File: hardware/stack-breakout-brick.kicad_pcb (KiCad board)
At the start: 2 copper layers, 40 x 40 mm, 10 parts, among them J1 STACK-UP-1, J2 STACK-DOWN-1, J3 STACK-UP-2, J4 STACK-DOWN-2, J5 CON-SERVO, J6 CON-SERVO, U1 DRILL, U2 DRILL, U3 DRILL, U4 DRILL

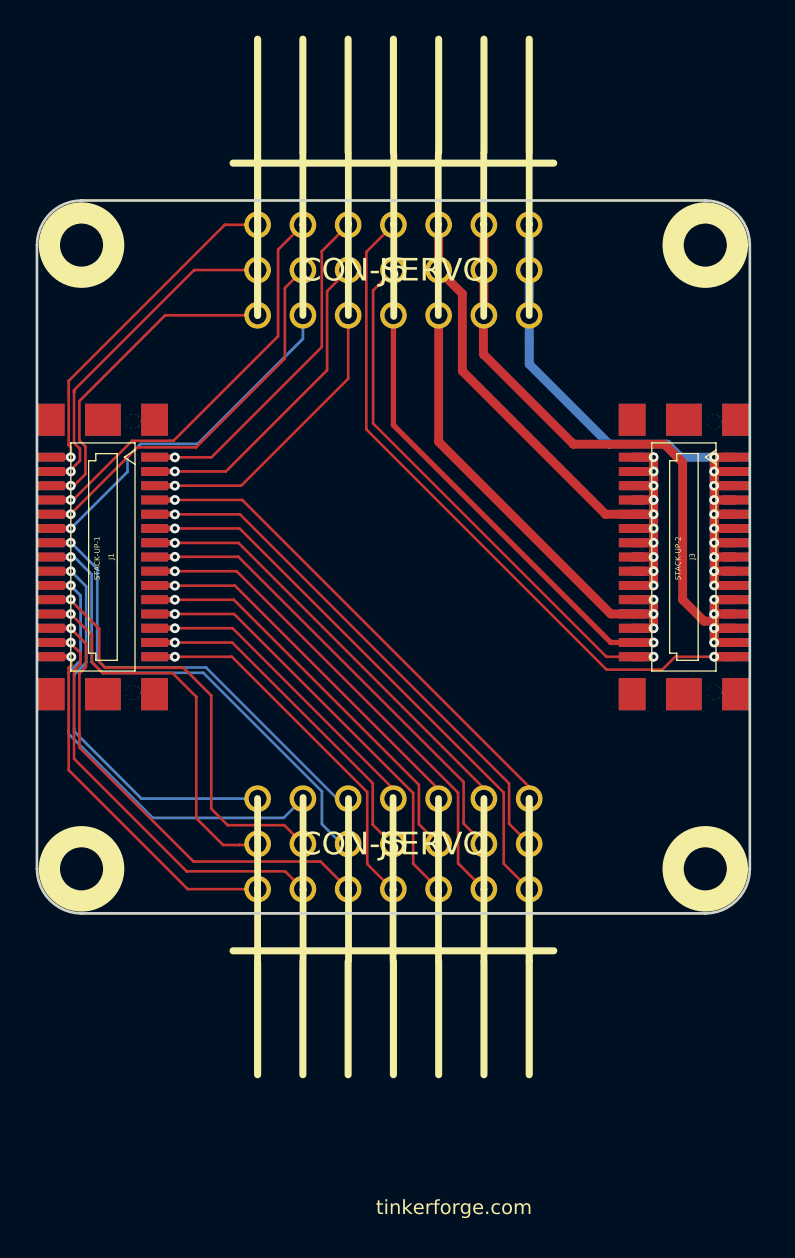
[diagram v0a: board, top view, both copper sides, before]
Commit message: Add pin labeling
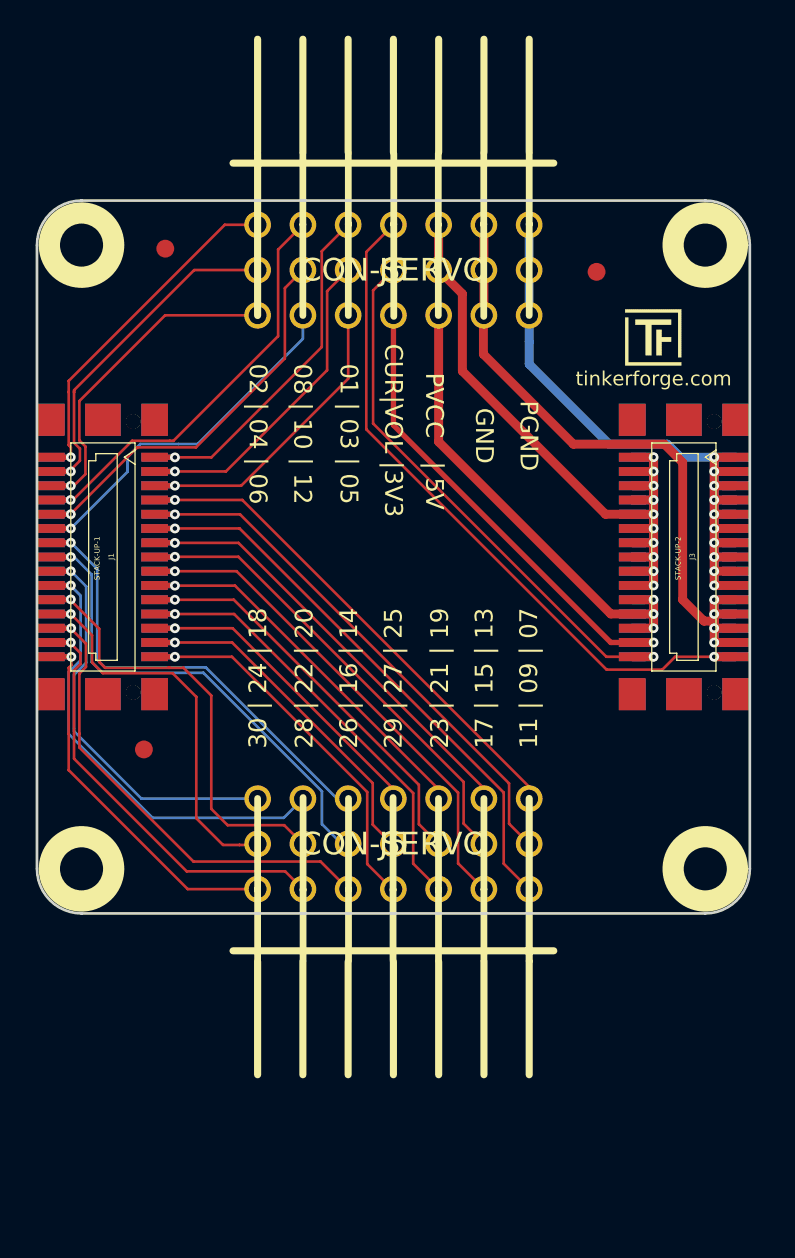
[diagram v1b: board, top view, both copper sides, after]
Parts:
- added Fiducial_Mark: VAL**, kicad-libraries:Fiducial_Mark, F.Cu at (125.5, 111.6)
- added Fiducial_Mark: VAL**, kicad-libraries:Fiducial_Mark, F.Cu at (150.9, 84.8)
- added Fiducial_Mark: VAL**, kicad-libraries:Fiducial_Mark, F.Cu at (126.7, 83.5)
- added G***: Logo_31x31, kicad-libraries:Logo_31x31, F.Cu at (152.5, 86.9)
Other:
- board text added: "01 | 03 | 05"
- board text added: "02 | 04 | 06"
- board text added: "08 | 10 | 12"
- board text added: "11 | 09 | 07"
- board text added: "17 | 15 | 13"
- board text added: "23 | 21 | 19"
- board text added: "26 | 16 | 14"
- board text added: "28 | 22 | 20"
- board text added: "29 | 27 | 25"
- board text added: "30 | 24 | 18"
- board text added: "CUR|VOL |3V3"
- board text added: "GND"
- board text added: "PGND"
- board text added: "PVCC | 5V"

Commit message: Add product name labeling
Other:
- board text added: "Stack Breakout Brick 1.0"
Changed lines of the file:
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@@
     (area 119.424999 80.724999 159.575001 120.875001)
     (thickness 1.6)
-    (drawings 23)
+    (drawings 24)
     (tracks 511)
     (zones 0)
@@
       (clearance 0.65024))
   )
+  (gr_text "Stack Breakout\nBrick 1.0" (at 153.9 112.9) (layer F.SilkS)
+    (effects (font (size 0.8 0.8) (thickness 0.15)))
+  )
   (gr_text PGND (at 147.1 94 270) (layer F.SilkS)

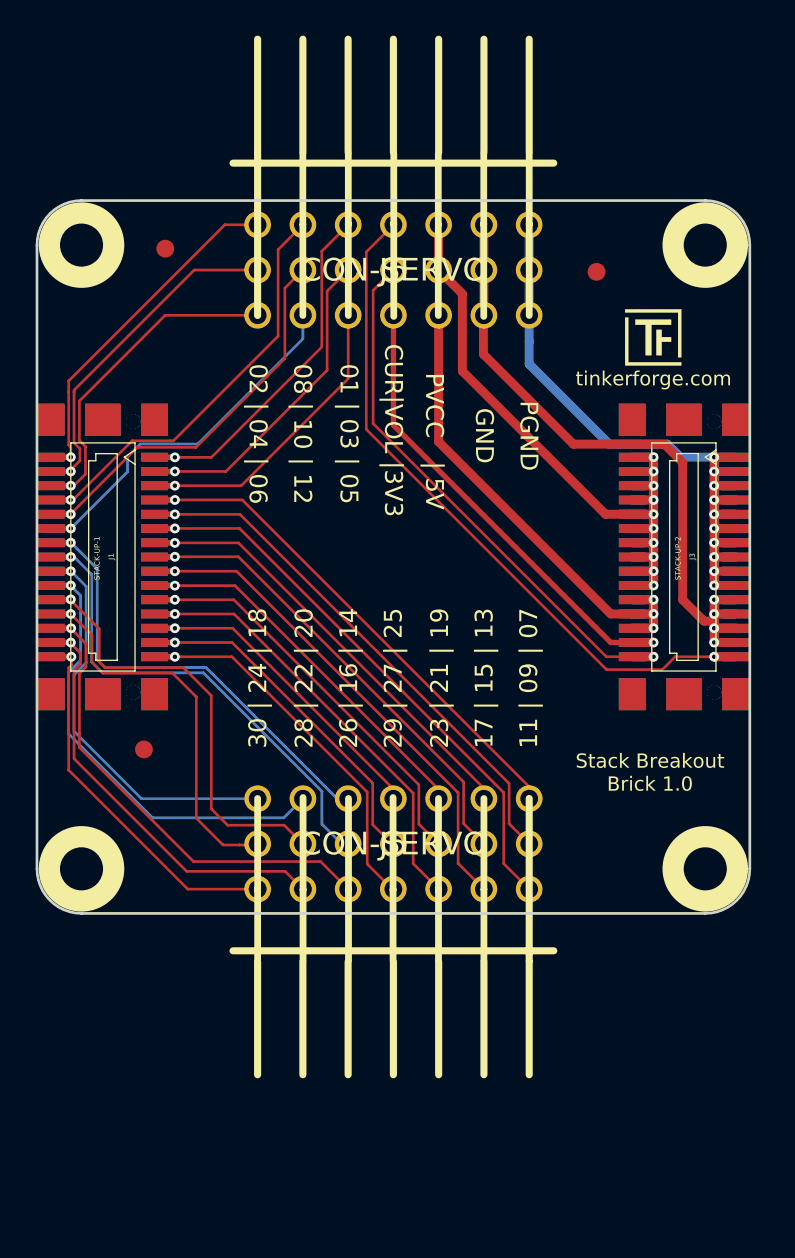
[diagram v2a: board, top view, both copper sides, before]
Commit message: Fix labeling and routing
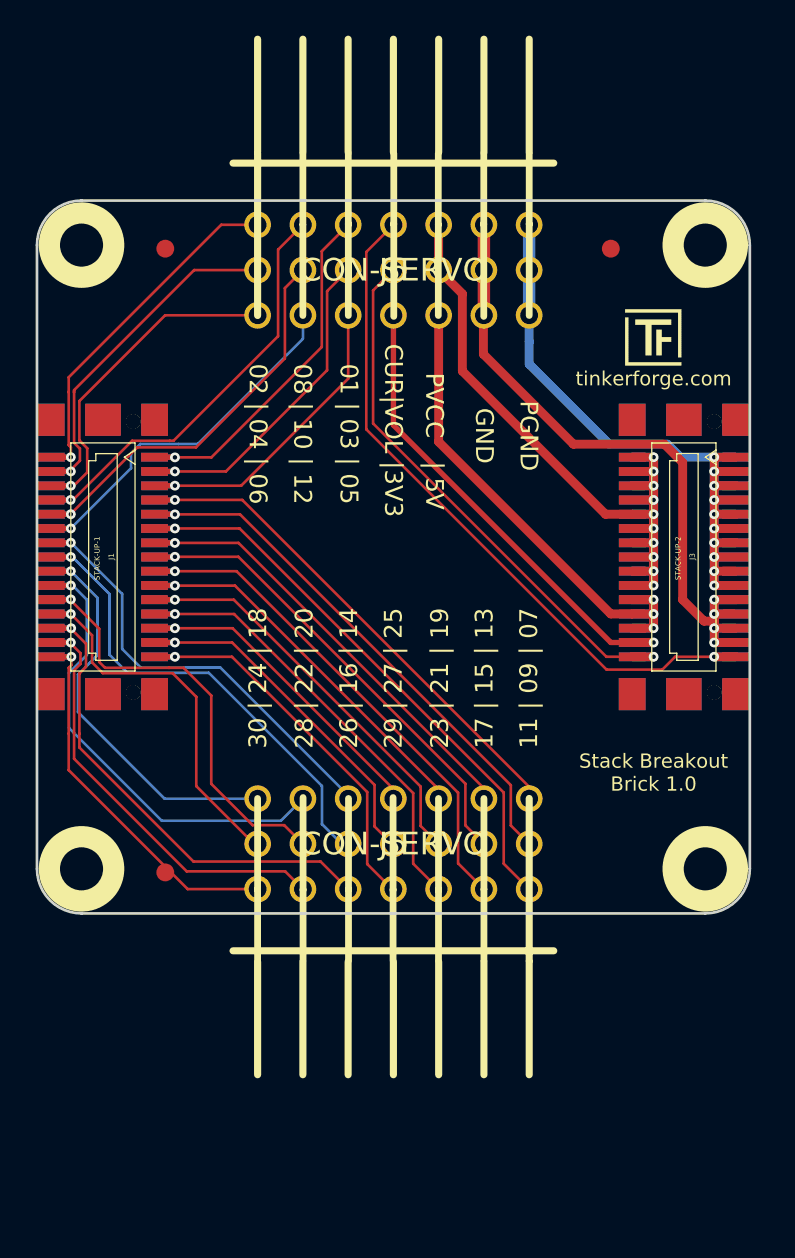
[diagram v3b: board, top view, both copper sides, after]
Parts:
- moved Fiducial_Mark 7.00 mm to (126.7, 118.5)
- moved Fiducial_Mark 1.53 mm to (151.7, 83.5)
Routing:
- net EX-SEL-01: track 23.0 -> 21.8 mm
- net EX-SEL-00: track 26.5 -> 25.7 mm
- net SEL-04: track 26.7 -> 25.9 mm
- net SEL-05: track 28.9 -> 28.2 mm

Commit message: Fix fiducial marks
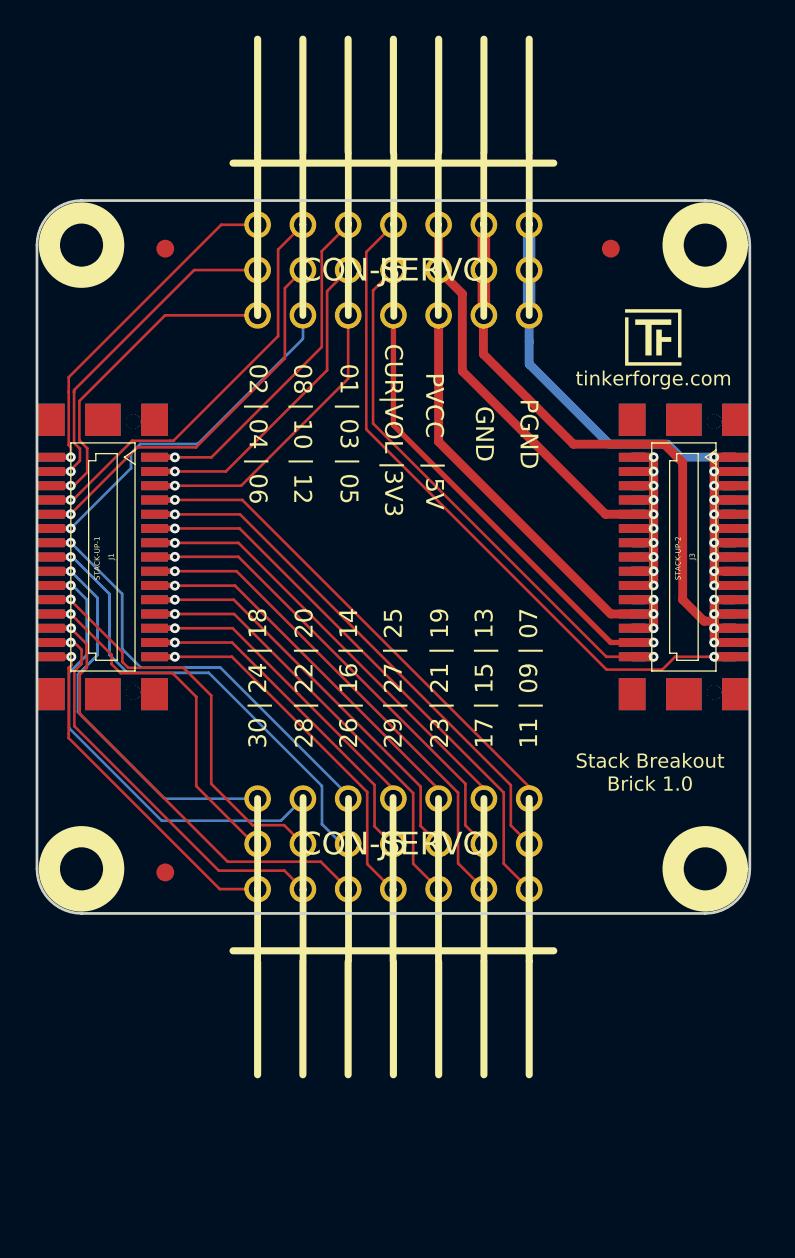
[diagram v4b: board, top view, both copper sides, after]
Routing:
- net EX-SER2-RXD: track 27.8 -> 26.7 mm
- net EX-SER2-RTS: track 22.2 -> 21.2 mm
- net EX-SER2-TXD: track 25.0 -> 24.0 mm
- net EX-SEL-00: track 25.7 -> 24.9 mm
- net EX-SEL-01: track 21.8 -> 21.2 mm
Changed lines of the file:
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@@
     (thickness 1.6)
     (drawings 24)
-    (tracks 505)
+    (tracks 503)
     (zones 0)
     (modules 14)
@@
   (title_block
     (title "Stack Breakout Brick")
-    (date 2017-03-01)
+    (date 2017-03-02)
     (rev 1.0)
     (company "Tinkerforge GmbH")
     (comment 1 "Licensed under CERN OHL v.1.1")
-    (comment 2 "Copyright (©) 2017, L.lauer <lukas.lauer@fh-bielefeld.de>")
+    (comment 2 "Copyright (©) 2017, L.Lauer <lukas.lauer@fh-bielefeld.de>")
   )
   (layers
@@
   )
   (setup
-    (last_trace_width 0.7)
+    (last_trace_width 0.25)
     (user_trace_width 0.15)
     (user_trace_width 0.2)
@@
     (effects (font (size 0.8 0.8) (thickness 0.15)))
   )
-  (gr_text "Stack Breakout\nBrick 1.0" (at 154.1 112.9) (layer F.SilkS)
+  (gr_text "Stack Breakout\nBrick 1.0" (at 153.9 112.9) (layer F.SilkS)
     (effects (font (size 0.8 0.8) (thickness 0.15)))
   )
-  (gr_text PGND (at 147.1 94 270) (layer F.SilkS)
+  (gr_text PGND (at 147.1 93.9 270) (layer F.SilkS)
     (effects (font (size 1 1) (thickness 0.2)))
   )
-  (gr_text GND (at 144.6 94 270) (layer F.SilkS)
+  (gr_text GND (at 144.6 93.9 270) (layer F.SilkS)
     (effects (font (size 1 1) (thickness 0.2)))
   )
@@
   (segment (start 127.724266 107.02) (end 129.28 108.575734) (width 0.15) (layer F.Cu) (net 27))
   (segment (start 121.4 103.18) (end 121.4 103.24) (width 0.15) (layer F.Cu) (net 27))
-  (segment (start 123.320002 107.02) (end 126.9 107.02) (width 0.15) (layer F.Cu) (net 27))
+  (segment (start 124.620002 107.02) (end 126.9 107.02) (width 0.15) (layer F.Cu) (net 27))
   (segment (start 126.9 107.02) (end 126.93 107.02) (width 0.15) (layer F.Cu) (net 27))
-  (segment (start 122.992133 106.692131) (end 123.320002 107.02) (width 0.15) (layer F.Cu) (net 27))
-  (segment (start 122.992133 104.832133) (end 122.992133 106.692131) (width 0.15) (layer F.Cu) (net 27))
-  (segment (start 121.4 103.24) (end 122.992133 104.832133) (width 0.15) (layer F.Cu) (net 27))
+  (segment (start 124.292133 106.692131) (end 124.620002 107.02) (width 0.15) (layer F.Cu) (net 27))
+  (segment (start 124.292133 106.132133) (end 124.292133 106.692131) (width 0.15) (layer F.Cu) (net 27))
+  (segment (start 121.4 103.24) (end 124.292133 106.132133) (width 0.15) (layer F.Cu) (net 27))
   (segment (start 120.31962 103.18) (end 121.4 103.18) (width 0.3) (layer B.Cu) (net 27))
   (segment (start 121.38224 103.19776) (end 121.4 103.18) (width 0.3) (layer F.Cu) (net 27))
@@
   (segment (start 120.30186 103.19776) (end 120.98776 103.19776) (width 0.15) (layer F.Cu) (net 27))
   (segment (start 131.82254 116.96) (end 131.88254 116.9) (width 0.15) (layer F.Cu) (net 28))
-  (segment (start 121.4 104) (end 122.59 105.19) (width 0.15) (layer F.Cu) (net 28))
+  (segment (start 121.4 104) (end 123.69 106.29) (width 0.15) (layer F.Cu) (net 28))
   (segment (start 128.44 113.66) (end 131.74 116.96) (width 0.15) (layer F.Cu) (net 28))
   (segment (start 128.44 108.65) (end 128.44 113.66) (width 0.15) (layer F.Cu) (net 28))
   (segment (start 127.110002 107.320002) (end 128.44 108.65) (width 0.15) (layer F.Cu) (net 28))
-  (segment (start 123.195738 107.320002) (end 127.110002 107.320002) (width 0.15) (layer F.Cu) (net 28))
-  (segment (start 122.59 106.714264) (end 123.195738 107.320002) (width 0.15) (layer F.Cu) (net 28))
-  (segment (start 122.59 105.19) (end 122.59 106.714264) (width 0.15) (layer F.Cu) (net 28))
+  (segment (start 124.195738 107.320002) (end 127.110002 107.320002) (width 0.15) (layer F.Cu) (net 28))
+  (segment (start 123.69 106.814264) (end 124.195738 107.320002) (width 0.15) (layer F.Cu) (net 28))
+  (segment (start 123.69 106.29) (end 123.69 106.814264) (width 0.15) (layer F.Cu) (net 28))
   (segment (start 120.304 104) (end 121.4 104) (width 0.3) (layer B.Cu) (net 28))
   (segment (start 121.39786 103.99786) (end 121.4 104) (width 0.15) (layer F.Cu) (net 28))
@@
   (segment (start 121.39786 103.99786) (end 120.30186 103.99786) (width 0.3) (layer F.Cu) (net 28))
   (segment (start 120.304 104) (end 120.30186 103.99786) (width 0.15) (layer B.Cu) (net 28))
-  (segment (start 121.880004 110.71) (end 121.880004 111.490002) (width 0.15) (layer F.Cu) (net 29))
-  (segment (start 121.42 104.84) (end 122.25 105.67) (width 0.15) (layer F.Cu) (net 29))
-  (segment (start 122.25 105.67) (end 122.25 106.970004) (width 0.15) (layer F.Cu) (net 29))
-  (segment (start 122.25 106.970004) (end 121.880004 107.34) (width 0.15) (layer F.Cu) (net 29))
-  (segment (start 121.880004 107.34) (end 121.880004 110.71) (width 0.15) (layer F.Cu) (net 29))
-  (segment (start 121.42 104.8) (end 121.42 104.84) (width 0.15) (layer F.Cu) (net 29))
-  (segment (start 135.41508 117.89) (end 136.96254 119.43746) (width 0.15) (layer F.Cu) (net 29))
-  (segment (start 128.280002 117.89) (end 135.41508 117.89) (width 0.15) (layer F.Cu) (net 29))
-  (segment (start 121.880004 111.490002) (end 128.280002 117.89) (width 0.15) (layer F.Cu) (net 29))
+  (segment (start 121.42 104.8) (end 121.42 104.82) (width 0.15) (layer F.Cu) (net 29))
+  (segment (start 135.42508 117.9) (end 136.96254 119.43746) (width 0.15) (layer F.Cu) (net 29))
+  (segment (start 130.2 117.9) (end 135.42508 117.9) (width 0.15) (layer F.Cu) (net 29))
+  (segment (start 121.9 109.6) (end 130.2 117.9) (width 0.15) (layer F.Cu) (net 29))
+  (segment (start 121.9 107.4) (end 121.9 109.6) (width 0.15) (layer F.Cu) (net 29))
+  (segment (start 122.3 107) (end 121.9 107.4) (width 0.15) (layer F.Cu) (net 29))
+  (segment (start 122.3 105.7) (end 122.3 107) (width 0.15) (layer F.Cu) (net 29))
+  (segment (start 121.42 104.82) (end 122.3 105.7) (width 0.15) (layer F.Cu) (net 29))
   (segment (start 120.3039 104.8) (end 121.42 104.8) (width 0.3) (layer F.Cu) (net 29))
   (segment (start 121.41796 104.79796) (end 121.42 104.8) (width 0.15) (layer B.Cu) (net 29))
@@
   (segment (start 121.41796 104.79796) (end 120.30186 104.79796) (width 0.3) (layer B.Cu) (net 29))
   (segment (start 120.3039 104.8) (end 120.30186 104.79796) (width 0.3) (layer F.Cu) (net 29))
-  (segment (start 121.580002 110.71) (end 121.580002 112.120002) (width 0.15) (layer F.Cu) (net 30))
-  (segment (start 121.4 105.66) (end 121.94 106.2) (width 0.15) (layer F.Cu) (net 30))
-  (segment (start 121.94 106.2) (end 121.94 106.800002) (width 0.15) (layer F.Cu) (net 30))
-  (segment (start 121.94 106.800002) (end 121.580002 107.16) (width 0.15) (layer F.Cu) (net 30))
-  (segment (start 121.580002 107.16) (end 121.580002 110.71) (width 0.15) (layer F.Cu) (net 30))
-  (segment (start 121.4 105.6) (end 121.4 105.66) (width 0.15) (layer F.Cu) (net 30))
-  (segment (start 133.42508 118.44) (end 134.42254 119.43746) (width 0.15) (layer F.Cu) (net 30))
-  (segment (start 127.9 118.44) (end 133.42508 118.44) (width 0.15) (layer F.Cu) (net 30))
-  (segment (start 121.580002 112.120002) (end 127.9 118.44) (width 0.15) (layer F.Cu) (net 30))
+  (segment (start 121.4 105.6) (end 121.6 105.6) (width 0.15) (layer F.Cu) (net 30))
+  (segment (start 133.38508 118.4) (end 134.42254 119.43746) (width 0.15) (layer F.Cu) (net 30))
+  (segment (start 129.7 118.4) (end 133.38508 118.4) (width 0.15) (layer F.Cu) (net 30))
+  (segment (start 121.599998 110.299998) (end 129.7 118.4) (width 0.15) (layer F.Cu) (net 30))
+  (segment (start 121.599998 107.200002) (end 121.599998 110.299998) (width 0.15) (layer F.Cu) (net 30))
+  (segment (start 121.999998 106.800002) (end 121.599998 107.200002) (width 0.15) (layer F.Cu) (net 30))
+  (segment (start 121.999998 105.999998) (end 121.999998 106.800002) (width 0.15) (layer F.Cu) (net 30))
+  (segment (start 121.6 105.6) (end 121.999998 105.999998) (width 0.15) (layer F.Cu) (net 30))
   (segment (start 120.3038 105.6) (end 121.4 105.6) (width 0.3) (layer B.Cu) (net 30))
   (segment (start 121.39806 105.59806) (end 120.30186 105.59806) (width 0.3) (layer F.Cu) (net 30))
@@
   (via (at 121.4 105.6) (size 0.55) (drill 0.25) (layers F.Cu B.Cu) (net 30))
   (segment (start 120.3038 105.6) (end 120.30186 105.59806) (width 0.15) (layer B.Cu) (net 30))
-  (segment (start 121.28 110.71) (end 121.28 112.76) (width 0.15) (layer F.Cu) (net 31))
+  (segment (start 121.28 110.71) (end 121.28 110.96) (width 0.15) (layer F.Cu) (net 31))
   (segment (start 121.43 106.87) (end 121.28 107.02) (width 0.15) (layer F.Cu) (net 31))
   (segment (start 121.28 107.02) (end 121.28 110.71) (width 0.15) (layer F.Cu) (net 31))
   (segment (start 121.43 106.4) (end 121.43 106.87) (width 0.15) (layer F.Cu) (net 31))
-  (segment (start 127.95746 119.43746) (end 131.88254 119.43746) (width 0.15) (layer F.Cu) (net 31))
-  (segment (start 121.28 112.76) (end 127.95746 119.43746) (width 0.15) (layer F.Cu) (net 31))
+  (segment (start 129.75746 119.43746) (end 131.88254 119.43746) (width 0.15) (layer F.Cu) (net 31))
+  (segment (start 121.28 110.96) (end 129.75746 119.43746) (width 0.15) (layer F.Cu) (net 31))
   (segment (start 120.3037 106.4) (end 121.43 106.4) (width 0.3) (layer B.Cu) (net 31))
   (segment (start 121.42816 106.39816) (end 121.43 106.4) (width 0.15) (layer F.Cu) (net 31))
